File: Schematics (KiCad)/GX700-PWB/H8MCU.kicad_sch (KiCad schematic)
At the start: 11 parts

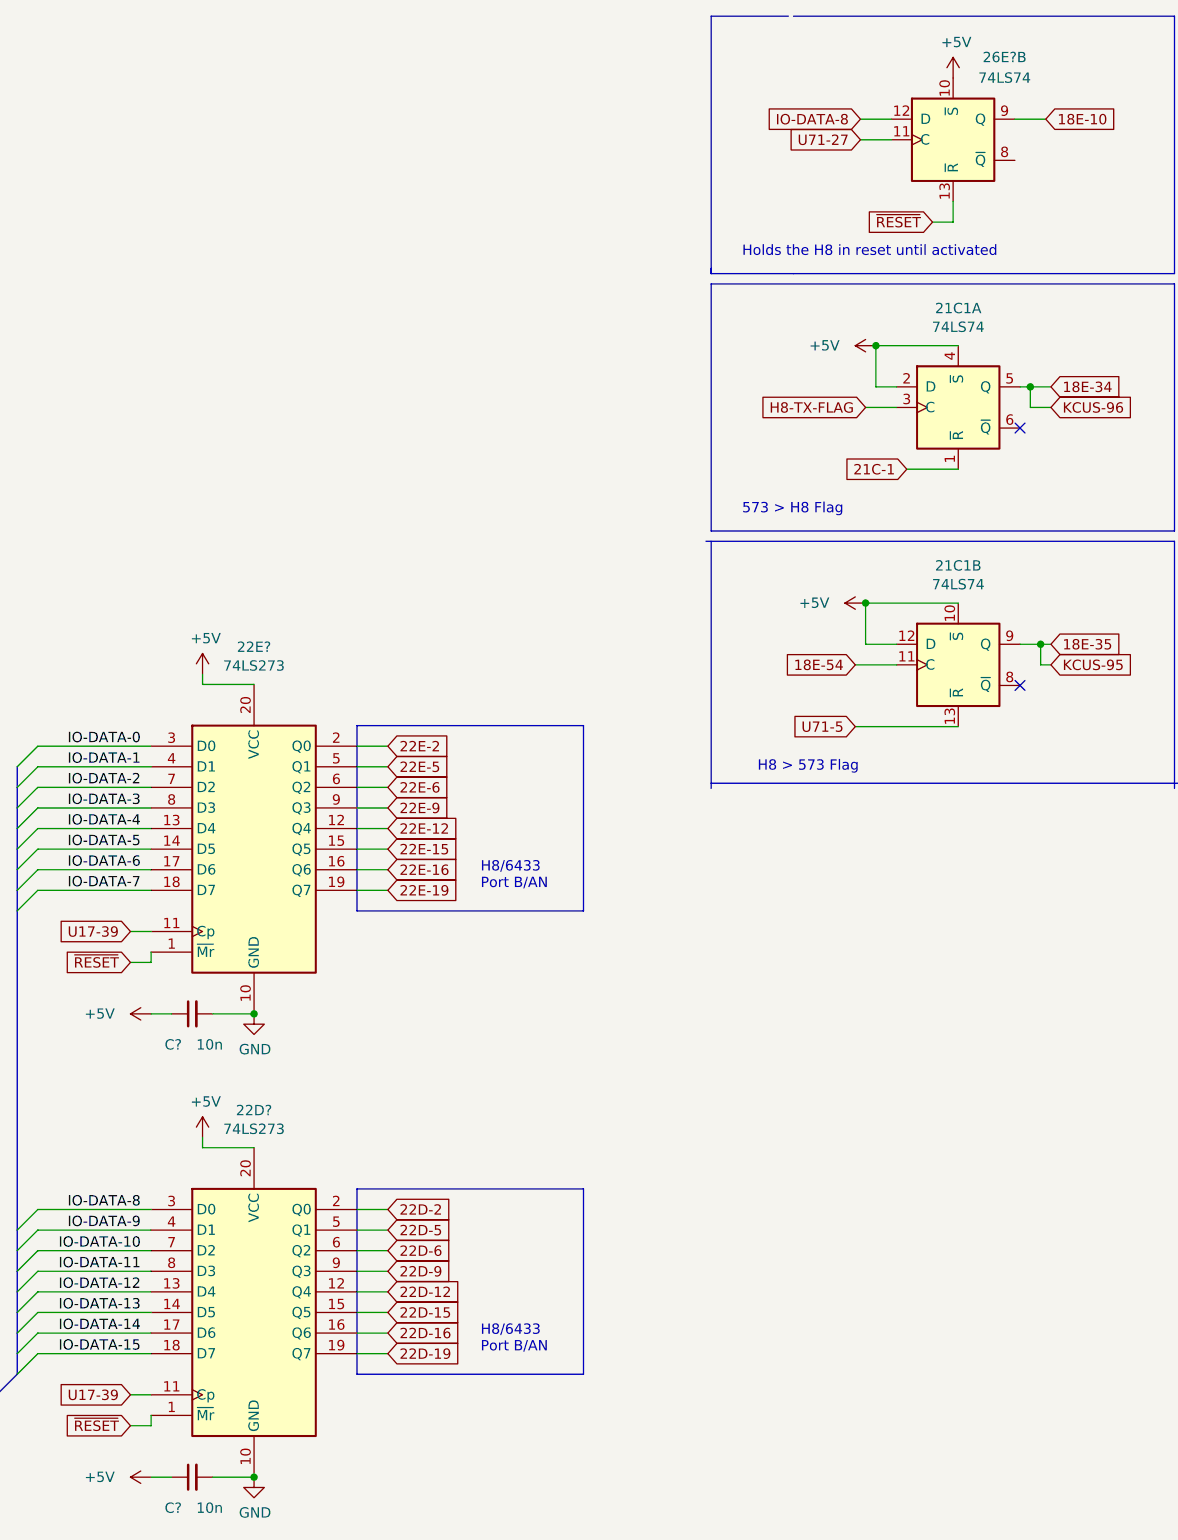
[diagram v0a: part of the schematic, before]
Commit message: Added Symbols, PSX page
Added PSX CPU and GPU symbols, added a COH PSX skeleton schematic and also updated the JAMMA symbol and footprint as it was bad.
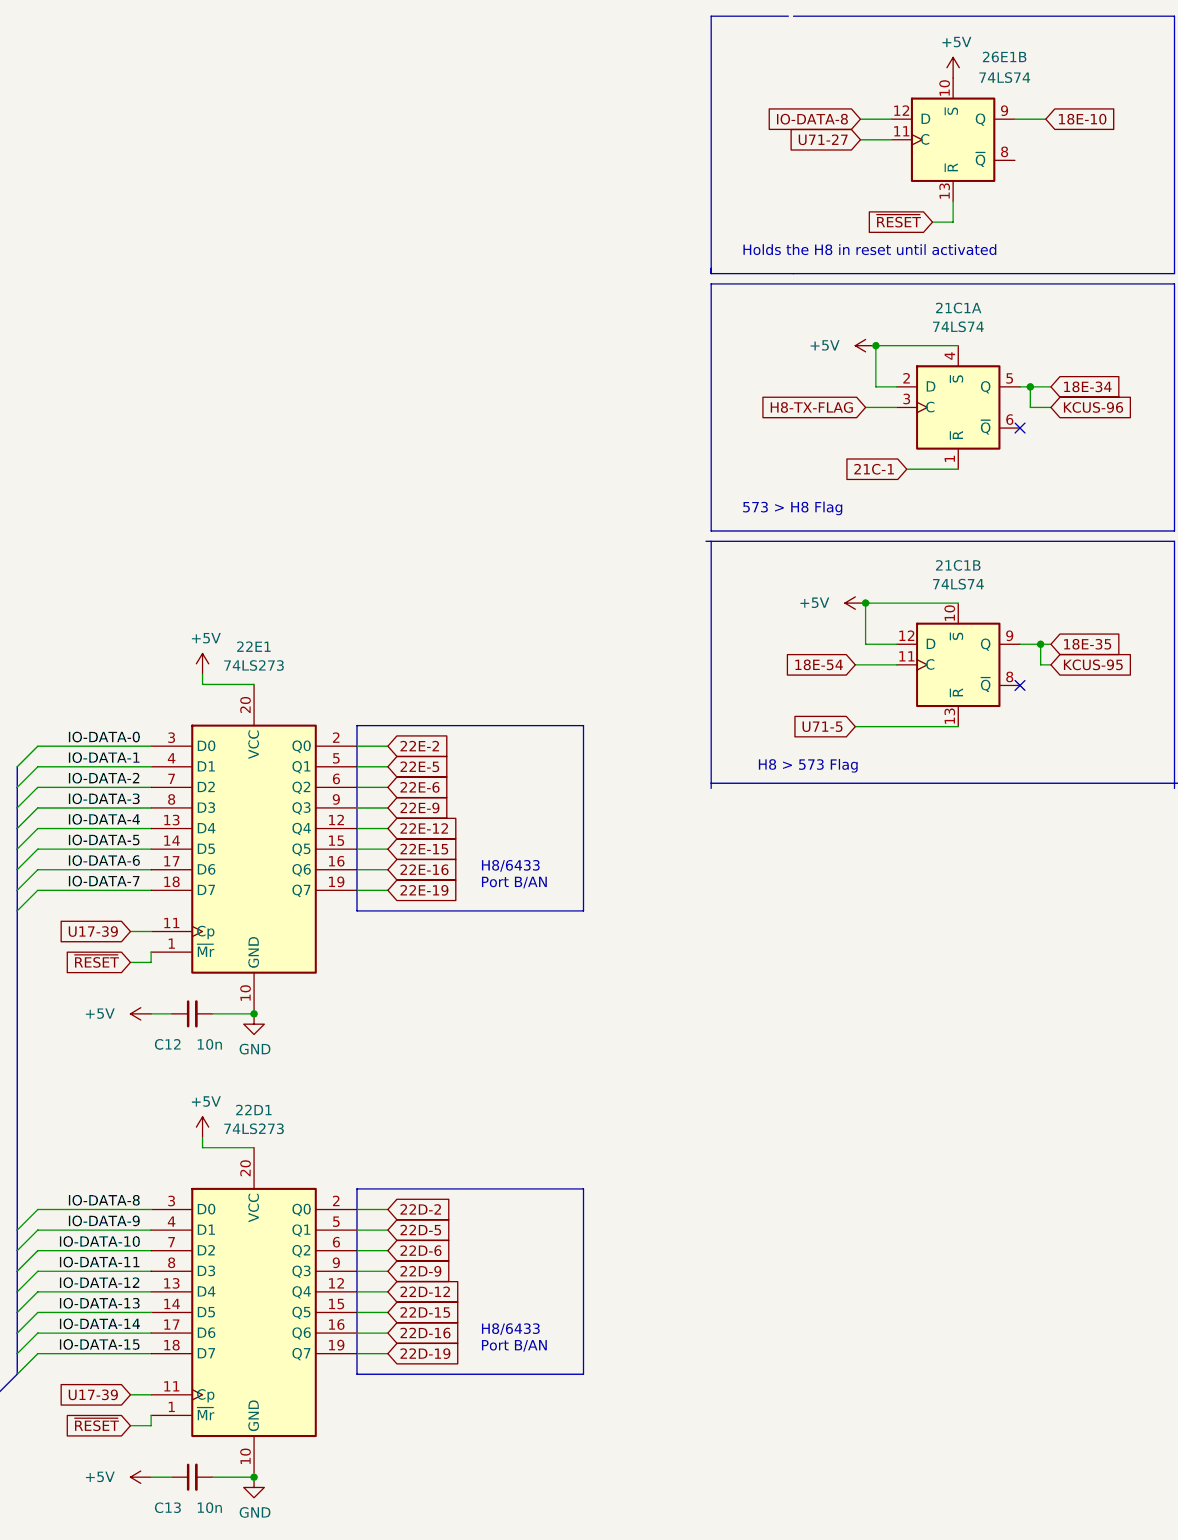
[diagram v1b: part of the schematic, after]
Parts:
- gave numbers to parts that had none: 5
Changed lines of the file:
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@@
   (symbol (lib_id "power:GND") (at 116.205 107.95 90) (unit 1)
     (in_bom yes) (on_board yes)
-    (property "Reference" "#PWR?" (id 0) (at 122.555 107.95 0)
+    (property "Reference" "#PWR0270" (id 0) (at 122.555 107.95 0)
       (effects (font (size 1.27 1.27)) hide)
     )
@@
   (symbol (lib_id "power:+5V") (at -43.053 100.203 0) (unit 1)
     (in_bom yes) (on_board yes)
-    (property "Reference" "#PWR?" (id 0) (at -43.053 104.013 0)
+    (property "Reference" "#PWR0272" (id 0) (at -43.053 104.013 0)
       (effects (font (size 1.27 1.27)) hide)
     )
@@
   (symbol (lib_id "power:GND") (at 116.205 54.61 0) (unit 1)
     (in_bom yes) (on_board yes)
-    (property "Reference" "#PWR?" (id 0) (at 116.205 60.96 0)
+    (property "Reference" "#PWR0268" (id 0) (at 116.205 60.96 0)
       (effects (font (size 1.27 1.27)) hide)
     )
@@
   (symbol (lib_id "power:+5V") (at 116.205 45.085 0) (unit 1)
     (in_bom yes) (on_board yes)
-    (property "Reference" "#PWR?" (id 0) (at 116.205 48.895 0)
+    (property "Reference" "#PWR0269" (id 0) (at 116.205 48.895 0)
       (effects (font (size 1.27 1.27)) hide)
     )
@@
   (symbol (lib_id "Device:C_Small") (at -44.323 199.263 90) (unit 1)
     (in_bom yes) (on_board yes)
-    (property "Reference" "C?" (id 0) (at -45.593 203.073 90)
+    (property "Reference" "C13" (id 0) (at -45.593 203.073 90)
       (effects (font (size 1.27 1.27)) (justify left))
     )
@@
   (symbol (lib_id "power:GND") (at -36.703 142.113 0) (unit 1)
     (in_bom yes) (on_board yes)
-    (property "Reference" "#PWR?" (id 0) (at -36.703 148.463 0)
+    (property "Reference" "#PWR0271" (id 0) (at -36.703 148.463 0)
       (effects (font (size 1.27 1.27)) hide)
     )
@@
   (symbol (lib_id "74xx:74LS74") (at 49.53 34.29 0) (unit 2)
     (in_bom yes) (on_board yes)
-    (property "Reference" "26E?" (id 0) (at 55.88 24.13 0))
+    (property "Reference" "26E1" (id 0) (at 55.88 24.13 0))
     (property "Value" "74LS74" (id 1) (at 55.88 26.67 0))
     (property "Footprint" "Package_SO:SO-14_5.3x10.2mm_P1.27mm" (id 2) (at 49.53 34.29 0)
@@
   (symbol (lib_id "power:+5V") (at -43.053 157.353 0) (unit 1)
     (in_bom yes) (on_board yes)
-    (property "Reference" "#PWR?" (id 0) (at -43.053 161.163 0)
+    (property "Reference" "#PWR0277" (id 0) (at -43.053 161.163 0)
       (effects (font (size 1.27 1.27)) hide)
     )
@@
   (symbol (lib_id "Device:C_Small") (at -44.323 142.113 90) (unit 1)
     (in_bom yes) (on_board yes)
-    (property "Reference" "C?" (id 0) (at -45.593 145.923 90)
+    (property "Reference" "C12" (id 0) (at -45.593 145.923 90)
       (effects (font (size 1.27 1.27)) (justify left))
     )
@@
   (symbol (lib_id "power:+5V") (at -49.403 142.113 90) (unit 1)
     (in_bom yes) (on_board yes)
-    (property "Reference" "#PWR?" (id 0) (at -45.593 142.113 0)
+    (property "Reference" "#PWR0276" (id 0) (at -45.593 142.113 0)
       (effects (font (size 1.27 1.27)) hide)
     )
@@
   (symbol (lib_id "power:+5V") (at -49.403 199.263 90) (unit 1)
     (in_bom yes) (on_board yes)
-    (property "Reference" "#PWR?" (id 0) (at -45.593 199.263 0)
+    (property "Reference" "#PWR0275" (id 0) (at -45.593 199.263 0)
       (effects (font (size 1.27 1.27)) hide)
     )
@@
   (symbol (lib_id "power:+5V") (at 49.53 26.67 0) (unit 1)
     (in_bom yes) (on_board yes)
-    (property "Reference" "#PWR?" (id 0) (at 49.53 30.48 0)
+    (property "Reference" "#PWR0273" (id 0) (at 49.53 30.48 0)
       (effects (font (size 1.27 1.27)) hide)
     )
@@
   (symbol (lib_id "74xx:74LS273") (at -36.703 121.793 0) (unit 1)
     (in_bom yes) (on_board yes)
-    (property "Reference" "22E?" (id 0) (at -36.703 96.8756 0))
+    (property "Reference" "22E1" (id 0) (at -36.703 96.8756 0))
     (property "Value" "74LS273" (id 1) (at -36.703 99.187 0))
     (property "Footprint" "Package_SO:SO-20_5.3x12.6mm_P1.27mm" (id 2) (at -36.703 121.793 0)
@@
   (symbol (lib_id "74xx:74LS273") (at -36.703 178.943 0) (unit 1)
     (in_bom yes) (on_board yes)
-    (property "Reference" "22D?" (id 0) (at -36.703 154.0256 0))
+    (property "Reference" "22D1" (id 0) (at -36.703 154.0256 0))
     (property "Value" "74LS273" (id 1) (at -36.703 156.337 0))
     (property "Footprint" "Package_SO:SO-20_5.3x12.6mm_P1.27mm" (id 2) (at -36.703 178.943 0)
@@
   (symbol (lib_id "power:GND") (at -36.703 199.263 0) (unit 1)
     (in_bom yes) (on_board yes)
-    (property "Reference" "#PWR?" (id 0) (at -36.703 205.613 0)
-      (effects (font (size 1.27 1.27)) hide)
-    )
+    (property "Reference" "#PWR0274" (id 0) (at -36.703 205.613 0)
+      (effects (font (size 1.27 1.27)) hide)
+    )

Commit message: General Fixes
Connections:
- net 18E-10 is gone; now on net H8-~{RST}: 26E1.9 (Q)
- net 18E-34: no longer 21C1.5 (Q)
- net 18E-35 renamed H8-RX-FLAG
- net 18E-54 renamed H8-RXF-CLK
- net 21C-1 renamed ~{H8-CLR-TXF}
- net H8-TX-FLAG renamed H8-WR-CLK
- net U71-27 renamed ~{H8-RST-CLK}
- net U71-5 renamed ~{H8-CLR-RXF}
- new net H8-WR: 21C1.5 (Q)
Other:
- moved on the sheet: 13E1C, 13E1E, 13E1F, 13E2D, 18E1, 21C1A, 21C1B, 22D1, 22E1, 26E1B, C12, C13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

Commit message: Major board changes to give a rough render of the PCB
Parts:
- 18E1: footprint Package_QFP:TQFP-64_10x10mm_P0.5mm -> Package_QFP:PQFP-64_14x14mm_P0.8mm
- renumbered 13E2 to 13E1
